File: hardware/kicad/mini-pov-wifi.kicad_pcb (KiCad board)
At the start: 2 copper layers, 28 x 118 mm, 24 parts, among them J2 USB-C, U1 MT3608, U2 Wemos_D1_Mini

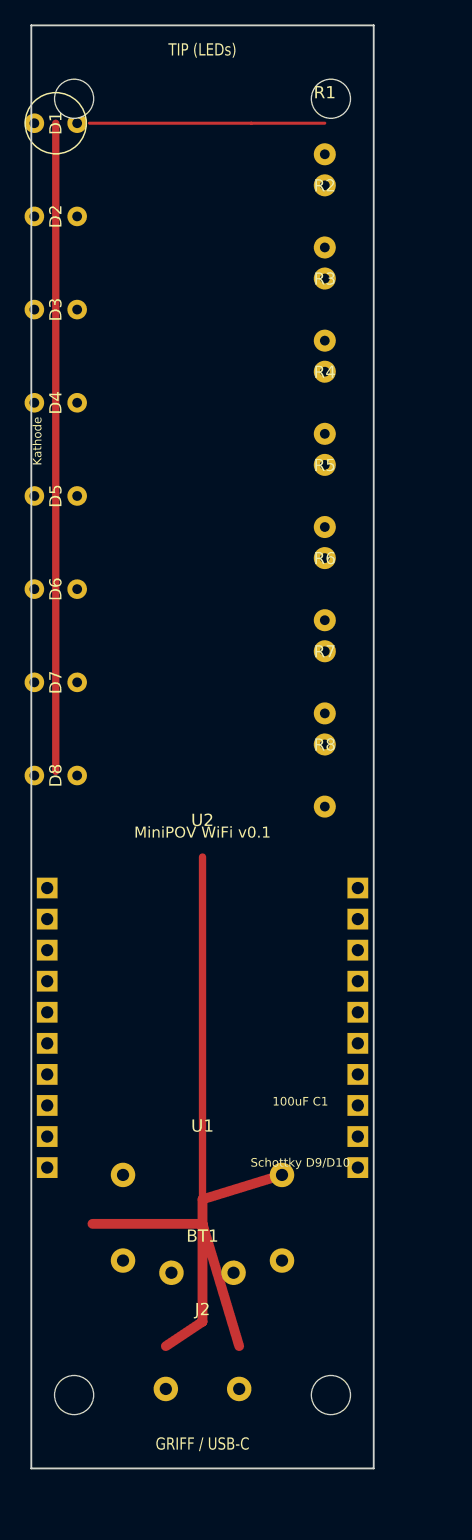
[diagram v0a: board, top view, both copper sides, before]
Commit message: Clean PCB layout: single LED column, readable silk labels, A/K marks.
Co-authored-by: Cursor <cursoragent@cursor.com>
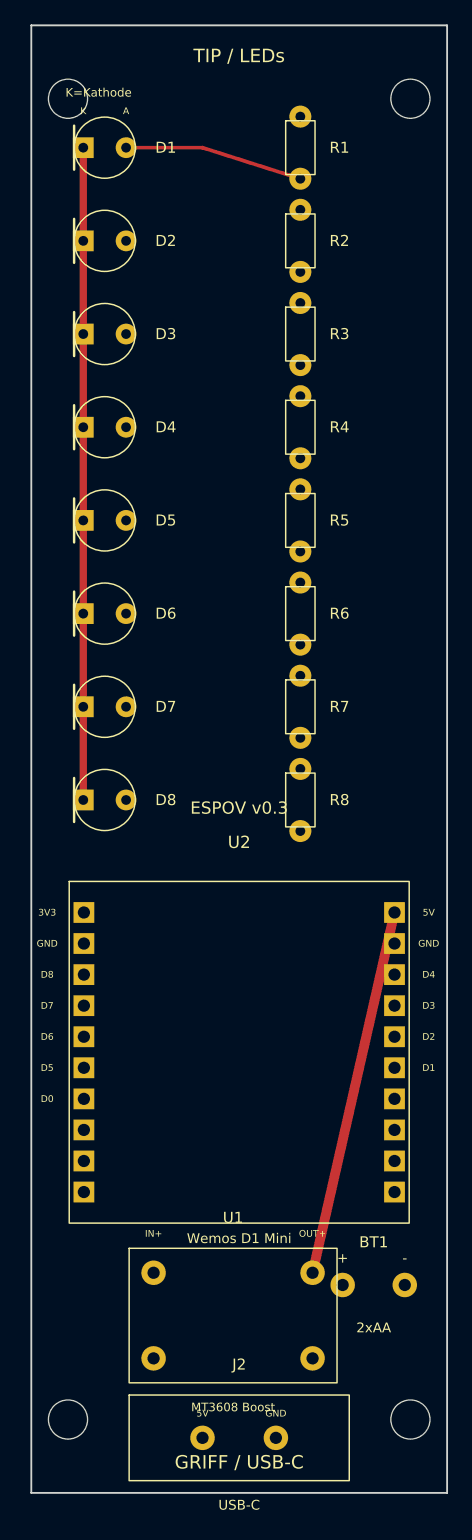
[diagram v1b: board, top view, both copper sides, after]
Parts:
- H1, H2, H3, H4: value MountingHole -> M3
- U1: value MT3608 -> MT3608 Boost
- U2: value Wemos_D1_Mini -> Wemos D1 Mini
- moved BT1 14.0 mm to (28.0, 103.0)
- moved U1 8.38 mm to (8.00, 100.0)
- moved H4 6.80 mm to (31.0, 114.0)
- moved H2 6.50 mm to (31.0, 6.00)
- moved J2 5.00 mm to (8.00, 112.0)
- moved D2 4.47 mm to (6.00, 17.6), turned to 0 degrees
- moved D1 4.47 mm to (6.00, 10.0), turned to 0 degrees
- moved D3 4.47 mm to (6.00, 25.2), turned to 0 degrees
- moved D4 4.47 mm to (6.00, 32.9), turned to 0 degrees
- moved D5 4.47 mm to (6.00, 40.5), turned to 0 degrees
- moved D6 4.47 mm to (6.00, 48.1), turned to 0 degrees
- moved D7 4.47 mm to (6.00, 55.7), turned to 0 degrees
- moved D8 4.47 mm to (6.00, 63.3), turned to 0 degrees
- moved U2 3.61 mm to (4.30, 70.0)
- moved R2 2.83 mm to (22.0, 17.6)
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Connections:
- R1 pad 1: LED1 -> GPIO_D1
- R1 pad 2: (no net) -> LED1
- R2 pad 1: LED2 -> GPIO_D2
- R2 pad 2: (no net) -> LED2
- R3 pad 1: LED3 -> GPIO_D4
- R3 pad 2: (no net) -> LED3
- R4 pad 1: LED4 -> GPIO_D5
- R4 pad 2: (no net) -> LED4
- R5 pad 1: LED5 -> GPIO_D6
- R5 pad 2: (no net) -> LED5
- R6 pad 1: LED6 -> GPIO_D7
- R6 pad 2: (no net) -> LED6
- R7 pad 1: LED7 -> GPIO_D8
- R7 pad 2: (no net) -> LED7
- R8 pad 1: LED8 -> GPIO_D0
- R8 pad 2: (no net) -> LED8
- U2 pad D0: (no net) -> GPIO_D0
- U2 pad D1: (no net) -> GPIO_D1
- U2 pad D2: (no net) -> GPIO_D2
- U2 pad D4: (no net) -> GPIO_D4
- U2 pad D5: (no net) -> GPIO_D5
- U2 pad D6: (no net) -> GPIO_D6
- U2 pad D7: (no net) -> GPIO_D7
- U2 pad D8: (no net) -> GPIO_D8
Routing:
- net GND: track 72.4 -> 53.3 mm
- net +5V: track 48.4 -> 30.2 mm
- net LED1: track 19.2 -> 14.6 mm
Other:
- board size 28 x 118 mm -> 34 x 120 mm
- board text added: "ESPOV v0.3"
- board text added: "K=Kathode"
- board text added: "TIP / LEDs"
- board text removed: "100uF C1"
- board text removed: "Kathode"
- board text removed: "MiniPOV WiFi v0.1"
- board text removed: "Schottky D9/D10"
- board text removed: "TIP (LEDs)"
